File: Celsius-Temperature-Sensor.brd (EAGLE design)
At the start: 6.3 x 41.3 mm, 19 parts, among them Q1 BSS138, Q2 BSS138

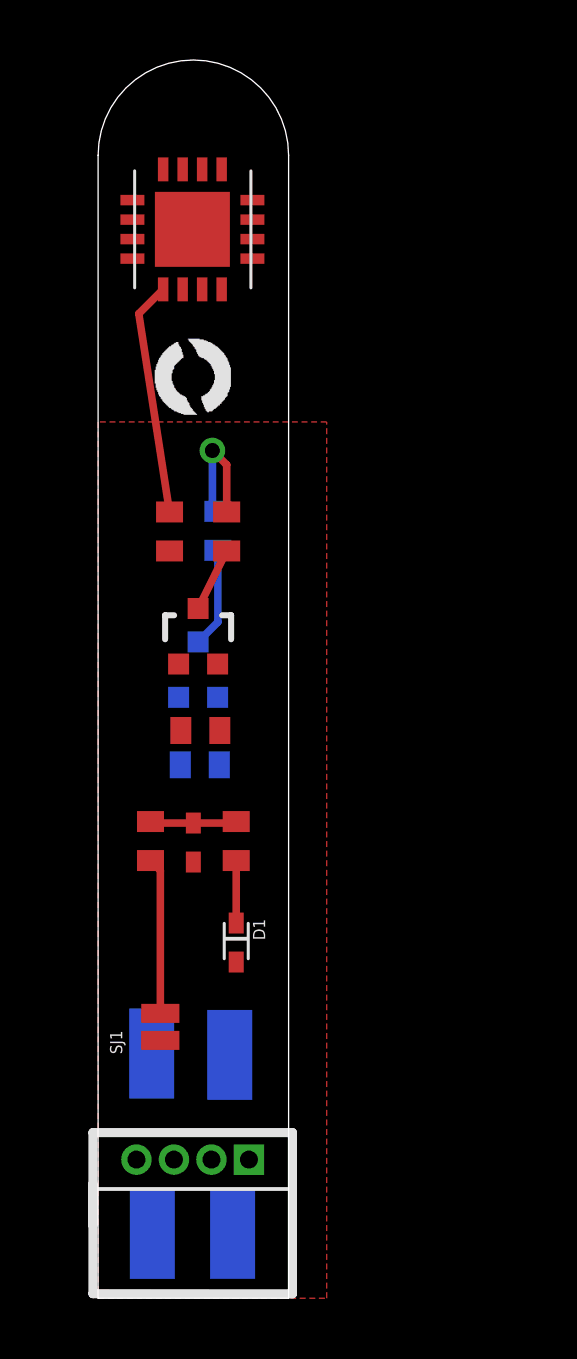
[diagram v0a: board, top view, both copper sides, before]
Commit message: Updated to new board outline. Still needs some fillets in the corners for machining.
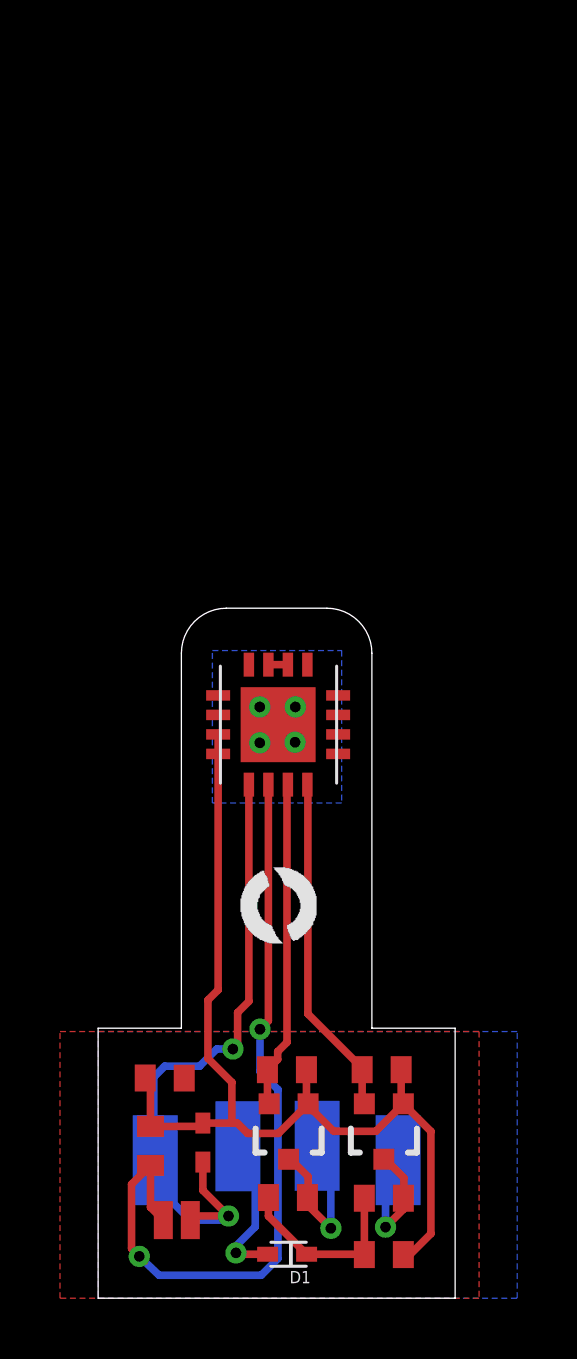
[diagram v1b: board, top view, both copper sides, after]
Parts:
- removed U$1: DF13-4P-1.25DS, con-hirose-df13:DF13-4P-1.25DS
- moved R3 22.8 mm to (9.53, 3.33), turned to 180 degrees
- moved R5 22.3 mm to (6.33, 3.36), flipped to the top, turned to 180 degrees
- moved C1 18.2 mm to (2.22, 7.34), turned to 0 degrees
- moved U$7 17.9 mm to (4.76, 11.8)
- moved Q1 17.6 mm to (9.53, 5.56), turned to 180 degrees
- moved U$8 16.8 mm to (6.00, 19.1)
- moved Q2 15.7 mm to (6.35, 5.56), flipped to the top, turned to 180 degrees
- moved R1 14.6 mm to (9.53, 1.46), turned to 0 degrees
- moved R2 12.8 mm to (9.45, 7.62), turned to 0 degrees
- moved D1 10.6 mm to (6.35, 1.47), turned to 180 degrees
- moved R4 10.6 mm to (6.29, 7.62), flipped to the top, turned to 0 degrees
- moved R6 10.2 mm to (1.75, 5.08)
- moved U$2 10.0 mm to (3.49, 5.24)
- moved U$6 8.95 mm to (10.0, 4.60)
- moved SJ1 6.46 mm to (2.62, 2.61), turned to 180 degrees
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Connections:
- new net TPAD: U$8.EXP
- net GND: no longer U$1.P$4
- net SCL_HV: no longer U$1.P$2
- net SDA_HV: no longer U$1.P$3
- net VIN: no longer U$1.P$1
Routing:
- net 3.3V: track 2.90 -> 33.4 mm
- net ADDR_SEL: track 5.23 -> 27.1 mm, vias 0 -> 2
- net GND: track 7.84 -> 22.3 mm, vias 0 -> 2
- net SDA_LV: track 0.00 -> 11.4 mm
- net SCL_LV: track 0.00 -> 10.9 mm
- net VIN: track 0.00 -> 5.13 mm, vias 0 -> 1
- net TPAD: track 0.00 -> 3.37 mm, vias 0 -> 4
- net SDA_HV: track 2.14 -> 5.22 mm, vias 0 -> 1
- net SCL_HV: track 3.32 -> 5.88 mm, vias 0 -> 1
- net N$1: track 0.00 -> 0.65 mm
- net VCC: track 6.43 -> 6.22 mm, vias 1 -> 0
- added copper zone on layer 16, net GND
- added copper zone on layer 16, net TPAD
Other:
- board size 6.3 x 41.3 mm -> 11.9 x 23 mm

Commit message: Updated frame.
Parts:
- moved U$7 2.82 mm to (7.57, 11.6), turned to 90 degrees
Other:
- board text added: "BLK GND"
- board text added: "BlueRobotics"
- board text added: "Celsius Temp Sensor"
- board text added: "GRN SCL"
- board text added: "RED VCC"
- board text added: "WHT SDA"
- board text added: "rev1"
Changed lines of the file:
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@@
 <layer number="27" name="tValues" color="7" fill="1" visible="yes" active="yes"/>
 <layer number="28" name="bValues" color="7" fill="1" visible="yes" active="yes"/>
-<layer number="29" name="tStop" color="7" fill="3" visible="no" active="yes"/>
-<layer number="30" name="bStop" color="7" fill="6" visible="no" active="yes"/>
+<layer number="29" name="tStop" color="7" fill="3" visible="yes" active="yes"/>
+<layer number="30" name="bStop" color="7" fill="6" visible="yes" active="yes"/>
 <layer number="31" name="tCream" color="7" fill="4" visible="no" active="yes"/>
 <layer number="32" name="bCream" color="7" fill="5" visible="no" active="yes"/>
@@
 <wire x1="11.90124375" y1="0.001228125" x2="11.90124375" y2="9.001228125" width="0.025" layer="20"/>
 <wire x1="0.00124375" y1="0.001228125" x2="11.90124375" y2="0.001228125" width="0.025" layer="20"/>
+<text x="2.9824625" y="6.444446875" size="0.8128" layer="22" rot="MR0">BLK
+GND</text>
+<text x="5.61671875" y="6.807515625" size="0.8128" layer="22" rot="MR0">RED
+VCC</text>
+<text x="8.3418125" y="6.83776875" size="0.8128" layer="22" rot="MR0">GRN
+SCL</text>
+<text x="10.97606875" y="6.414190625" size="0.8128" layer="22" rot="MR0">WHT
+SDA</text>
+<text x="7.8272625" y="17.26083125" size="0.8128" layer="21" rot="R270">BlueRobotics</text>
+<text x="3.97615625" y="13.02396875" size="0.6096" layer="21" rot="R90" align="center">Celsius Temp
+Sensor</text>
+<text x="6.032265625" y="22.13015625" size="0.6096" layer="21" align="center">rev1</text>
 </plain>
 <attributes>
@@
 <element name="U$5" library="BR-Eagle-Library" package="PAD-1.5X3MM" value="PAD1.5X3MM" x="7.3025" y="5.08" rot="MR270"/>
 <element name="U$6" library="BR-Eagle-Library" package="PAD-1.5X3MM" value="PAD1.5X3MM" x="10.00125" y="4.60375" rot="MR270"/>
-<element name="U$7" library="BR-Eagle-Library" package="BR-LOGO-SMALL" value="LOGOBR-LOGO-S" x="4.759621875" y="11.840525"/>
+<element name="U$7" library="BR-Eagle-Library" package="BR-LOGO-SMALL" value="LOGOBR-LOGO-S" x="7.573475" y="11.63916875" rot="R90"/>
 <element name="U$8" library="BR-Eagle-Library" package="QFN16-4X4" value="TSYS01QFN" x="6.0009625" y="19.11965625" smashed="yes" rot="R90"/>
 <element name="SJ1" library="SparkFun-Passives" package="PAD-JUMPER-2-NO_NO_SILK" value="JUMPER-PAD-2-NO" x="2.62366875" y="2.605415625" smashed="yes" rot="R180"/>
@@
 <wire x1="4.0009625" y1="18.79465625" x2="4.0009625" y2="18.14465625" width="0.254" layer="1"/>
 <wire x1="4.45944375" y1="5.87345625" x2="4.49415" y2="5.83875" width="0.254" layer="1"/>
-<wire x1="4.0009625" y1="18.14465625" x2="4.0009625" y2="10.277678125" width="0.254" layer="1"/>
-<wire x1="4.0009625" y1="10.277678125" x2="3.66125625" y2="9.937971875" width="0.254" layer="1"/>
-<wire x1="3.66125625" y1="9.937971875" x2="3.66125625" y2="7.995846875" width="0.254" layer="1"/>
 <wire x1="3.66125625" y1="7.995846875" x2="4.45944375" y2="7.197659375" width="0.254" layer="1"/>
 <wire x1="4.45944375" y1="7.197659375" x2="4.45944375" y2="5.87345625" width="0.254" layer="1"/>
+<wire x1="3.66125625" y1="7.995846875" x2="3.66125625" y2="9.442159375" width="0.254" layer="1"/>
+<wire x1="3.66125625" y1="9.442159375" x2="4.3636" y2="10.144503125" width="0.254" layer="1"/>
+<wire x1="4.3636" y1="10.144503125" x2="4.3636" y2="16.605378125" width="0.254" layer="1"/>
+<wire x1="4.3636" y1="16.605378125" x2="4.0078" y2="16.961178125" width="0.254" layer="1"/>
+<wire x1="4.0078" y1="16.961178125" x2="4.0078" y2="18.13781875" width="0.254" layer="1"/>
+<wire x1="4.0078" y1="18.13781875" x2="4.0009625" y2="18.14465625" width="0.254" layer="1"/>
 </signal>
 <signal name="VCC">
@@
 </board>
 </drawing>
+<compatibility>
+<note version="6.3" minversion="6.2.2" severity="warning">
+Since Version 6.2.2 text objects can contain more than one line,
+which will not be processed correctly with this version.
+</note>
+</compatibility>
 </eagle>

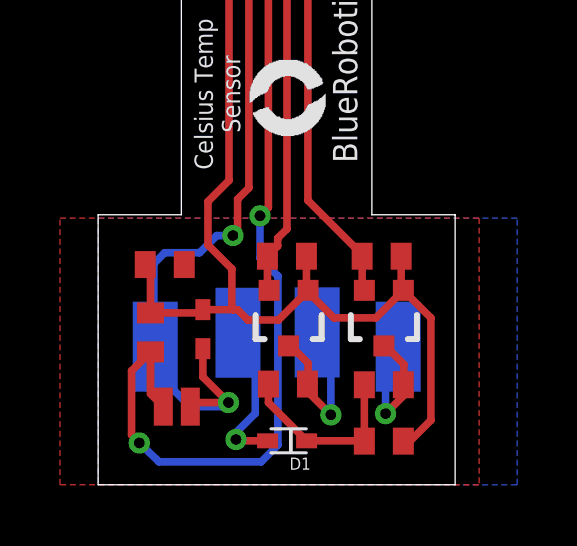
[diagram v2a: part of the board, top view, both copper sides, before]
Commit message: Updated zener to LDO.
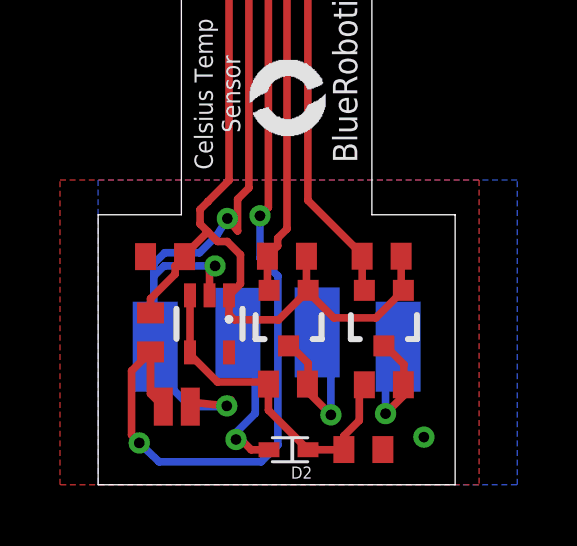
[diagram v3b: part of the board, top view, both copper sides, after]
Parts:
- removed C1: 0.1uF, resistor:C0402
- removed D1: (no value), SparkFun-DiscreteSemi:SOD523
- removed R1: 1K, resistor:R0402
- removed U$2: 3.3V 100mW, BR-Eagle-Library:SOD523
- added C2, C3: 1uF, resistor:C0402
- added D2: (no value), SparkFun-DiscreteSemi:SOD523
- added U$1: VREG-MIC5365, BlueRobotics-Main:SC70-5L
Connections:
- net 3.3V: now also C2.1, U$1.1; no longer C1.1, R1.2, U$2.C
- net GND: now also C2.2, C3.2, U$1.2; no longer C1.2, U$2.A
- net VCC: now also C3.1, D2.C, U$1.3, U$1.4; no longer D1.C, R1.1
- net VIN: now also D2.A; no longer D1.A
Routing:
- net 3.3V: track 33.7 -> 27.6 mm
- net VCC: track 6.22 -> 11.4 mm
- net GND: track 22.3 -> 23.8 mm, vias 2 -> 4

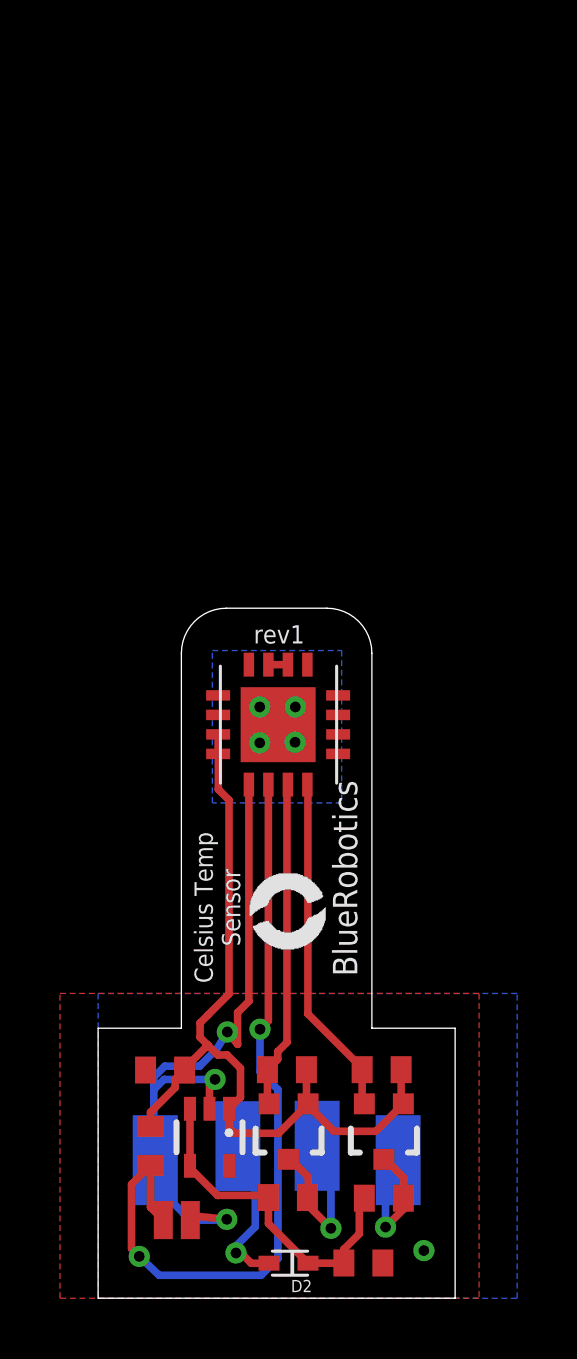
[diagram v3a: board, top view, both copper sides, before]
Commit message: Fixed incorrect regulator footprint. Stupid mistake.
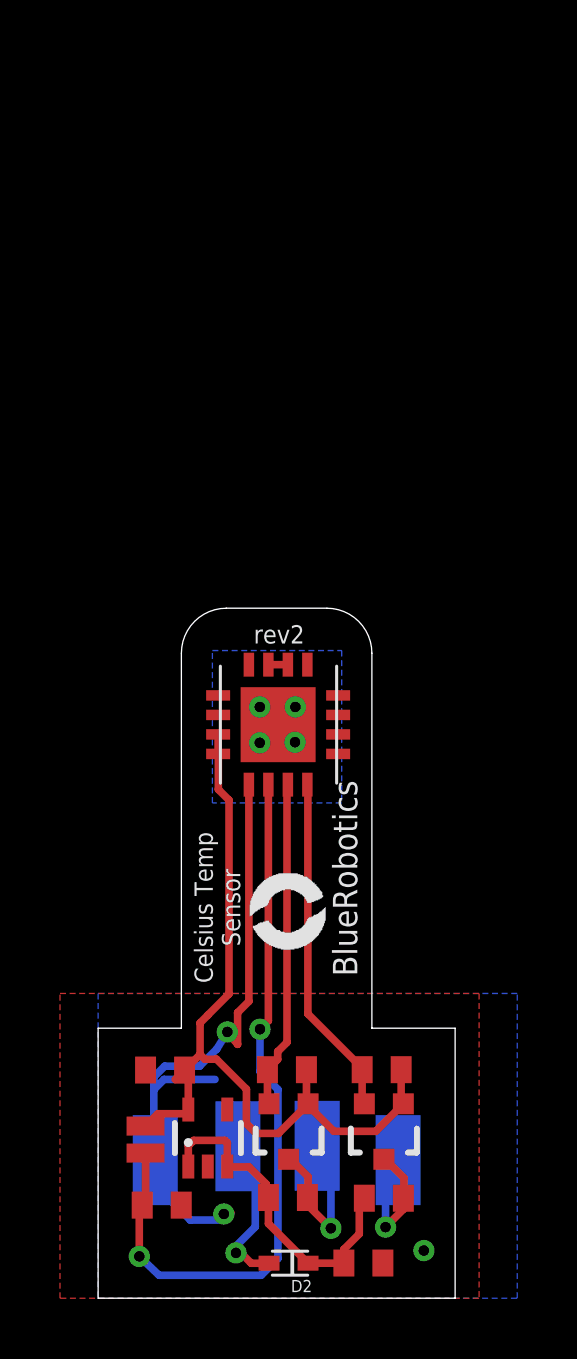
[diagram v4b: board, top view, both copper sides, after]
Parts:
- moved SJ1 2.88 mm to (1.58, 5.29), turned to 90 degrees
- moved R6 2.01 mm to (2.12, 3.10), turned to 180 degrees
- moved U$1 0.06 mm to (3.66, 5.34), turned to 0 degrees
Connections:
- net 3.3V: now also SJ1.2, U$1.5; no longer R6.2, U$1.1
- net ADDR_SEL: now also R6.2, SJ1.1; no longer R6.1, SJ1.2
- net GND: now also R6.1; no longer SJ1.1
- net VCC: now also U$1.1; no longer U$1.4
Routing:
- net GND: track 23.8 -> 21.5 mm, vias 4 -> 3
- net ADDR_SEL: track 27.1 -> 25.0 mm
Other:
- board text added: "rev2"
- board text removed: "rev1"

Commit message: Removed diode because it caused a large enough Vf to drop voltage outside of range needed to achieve high accuracy Acc1. Also added a few ground vias. Ordering production version from this revision.
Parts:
- removed D2: (no value), SparkFun-DiscreteSemi:SOD523
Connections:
- removed net VIN: D2.A, U$4.P$1
- net VCC: now also U$4.P$1; no longer D2.C
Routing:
- net VCC: track 11.3 -> 17.4 mm, vias 0 -> 1
- net VIN: track 5.31 -> 0.00 mm, vias 1 -> 0
- net GND: vias 3 -> 6
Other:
- board text added: "rev3"
- board text removed: "rev2"
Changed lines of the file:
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@@
 <text x="3.97615625" y="13.02396875" size="0.6096" layer="21" rot="R90" align="center">Celsius Temp
 Sensor</text>
-<text x="6.032265625" y="22.13015625" size="0.6096" layer="21" align="center">rev2</text>
+<text x="6.032265625" y="22.13015625" size="0.6096" layer="21" align="center">rev3</text>
 </plain>
 <attributes>
@@
 <element name="R6" library="resistor" package="R0402" value="10K" x="2.1214875" y="3.10378125" smashed="yes" rot="R180"/>
 <element name="C2" library="resistor" package="C0402" value="1uF" x="2.231546875" y="7.606090625" smashed="yes" rot="R180"/>
-<element name="D2" library="SparkFun-DiscreteSemi" package="SOD523" value="" x="6.39688125" y="1.168859375" rot="R180"/>
 <element name="U$1" library="BlueRobotics-Main" package="SC70-5L" value="VREG-MIC5365" x="3.656909375" y="5.33935625" smashed="yes"/>
 <element name="C3" library="resistor" package="C0402" value="1uF" x="8.8427125" y="1.174790625" smashed="yes"/>
@@
 <wire x1="2.196903125" y1="7.294328125" x2="1.85763125" y2="6.95505625" width="0.254" layer="16"/>
 <contactref element="R6" pad="1"/>
+<via x="6.7773875" y="2.036903125" extent="1-16" drill="0.3556"/>
+<via x="0.7627" y="6.689925" extent="1-16" drill="0.3556"/>
+<via x="11.1122125" y="7.43325" extent="1-16" drill="0.3556"/>
 </signal>
 <signal name="SCL_LV">
@@
 <contactref element="R3" pad="2"/>
 <contactref element="R5" pad="2"/>
-<wire x1="5.67810625" y1="3.357140625" x2="5.67810625" y2="2.487634375" width="0.254" layer="1"/>
-<contactref element="D2" pad="C"/>
 <contactref element="U$1" pad="1"/>
 <contactref element="U$1" pad="3"/>
 <contactref element="C3" pad="1"/>
 <wire x1="5.607803125" y1="3.42744375" x2="5.67810625" y2="3.357140625" width="0.254" layer="1"/>
-<wire x1="6.99688125" y1="1.168859375" x2="8.18678125" y2="1.168859375" width="0.254" layer="1"/>
 <wire x1="8.18678125" y1="1.168859375" x2="8.1927125" y2="1.174790625" width="0.254" layer="1"/>
 <wire x1="8.1927125" y1="1.174790625" x2="8.1927125" y2="1.631784375" width="0.254" layer="1"/>
@@
 <wire x1="8.705840625" y1="2.1449125" x2="8.705840625" y2="3.164590625" width="0.254" layer="1"/>
 <wire x1="8.705840625" y1="3.164590625" x2="8.875" y2="3.33375" width="0.254" layer="1"/>
-<wire x1="5.67810625" y1="2.487634375" x2="6.99688125" y2="1.168859375" width="0.254" layer="1"/>
 <wire x1="5.607803125" y1="3.42744375" x2="5.607803125" y2="3.8031875" width="0.254" layer="1"/>
 <wire x1="5.607803125" y1="3.8031875" x2="5.032" y2="4.378990625" width="0.254" layer="1"/>
@@
 <wire x1="4.307971875" y1="5.182409375" x2="4.307971875" y2="4.39041875" width="0.254" layer="1"/>
 <wire x1="4.307971875" y1="4.39041875" x2="4.306909375" y2="4.38935625" width="0.254" layer="1"/>
+<wire x1="5.67810625" y1="3.357140625" x2="5.67810625" y2="1.195365625" width="0.254" layer="1"/>
+<wire x1="5.67810625" y1="1.195365625" x2="5.682209375" y2="1.1912625" width="0.254" layer="1"/>
+<wire x1="5.682209375" y1="1.1912625" x2="8.176240625" y2="1.1912625" width="0.254" layer="1"/>
+<wire x1="8.176240625" y1="1.1912625" x2="8.1927125" y2="1.174790625" width="0.254" layer="1"/>
+<contactref element="U$4" pad="P$1"/>
+<wire x1="4.64099375" y1="1.466015625" x2="4.59575625" y2="1.511253125" width="0.254" layer="1"/>
+<via x="4.59575625" y="1.511253125" extent="1-16" drill="0.3556"/>
+<wire x1="4.59575625" y1="1.511253125" x2="4.59575625" y2="1.737859375" width="0.254" layer="16"/>
+<wire x1="4.59575625" y1="1.737859375" x2="5.23904375" y2="2.381146875" width="0.254" layer="16"/>
+<wire x1="5.23904375" y1="2.381146875" x2="5.23904375" y2="4.487240625" width="0.254" layer="16"/>
+<wire x1="5.23904375" y1="4.487240625" x2="4.660484375" y2="5.0658" width="0.254" layer="16"/>
+<wire x1="4.64099375" y1="1.466015625" x2="4.80433125" y2="1.466015625" width="0.254" layer="1"/>
+<wire x1="4.80433125" y1="1.466015625" x2="5.103425" y2="1.166921875" width="0.254" layer="1"/>
+<wire x1="5.103425" y1="1.166921875" x2="5.69494375" y2="1.166921875" width="0.254" layer="1"/>
+<wire x1="5.69494375" y1="1.166921875" x2="5.69494375" y2="1.178528125" width="0.254" layer="1"/>
+<wire x1="5.69494375" y1="1.178528125" x2="5.682209375" y2="1.1912625" width="0.254" layer="1"/>
 </signal>
 <signal name="SCL_HV">
@@
 <wire x1="6.9987625" y1="3.377796875" x2="6.97810625" y2="3.357140625" width="0.254" layer="1"/>
 </signal>
-<signal name="VIN">
-<contactref element="U$4" pad="P$1"/>
-<wire x1="4.64099375" y1="1.466015625" x2="4.59575625" y2="1.511253125" width="0.254" layer="1"/>
-<via x="4.59575625" y="1.511253125" extent="1-16" drill="0.3556"/>
-<wire x1="4.59575625" y1="1.511253125" x2="4.59575625" y2="1.737859375" width="0.254" layer="16"/>
-<wire x1="4.59575625" y1="1.737859375" x2="5.23904375" y2="2.381146875" width="0.254" layer="16"/>
-<wire x1="5.23904375" y1="2.381146875" x2="5.23904375" y2="4.487240625" width="0.254" layer="16"/>
-<wire x1="5.23904375" y1="4.487240625" x2="4.660484375" y2="5.0658" width="0.254" layer="16"/>
-<contactref element="D2" pad="A"/>
-<wire x1="4.64099375" y1="1.466015625" x2="4.80433125" y2="1.466015625" width="0.254" layer="1"/>
-<wire x1="4.80433125" y1="1.466015625" x2="5.103425" y2="1.166921875" width="0.254" layer="1"/>
-<wire x1="5.103425" y1="1.166921875" x2="5.69494375" y2="1.166921875" width="0.254" layer="1"/>
-<wire x1="5.69494375" y1="1.166921875" x2="5.69688125" y2="1.168859375" width="0.254" layer="1"/>
-</signal>
 <signal name="N$1">
